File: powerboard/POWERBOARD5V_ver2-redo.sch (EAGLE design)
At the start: 37 parts, among them IC1 TPS5420, IC2 TPS5420

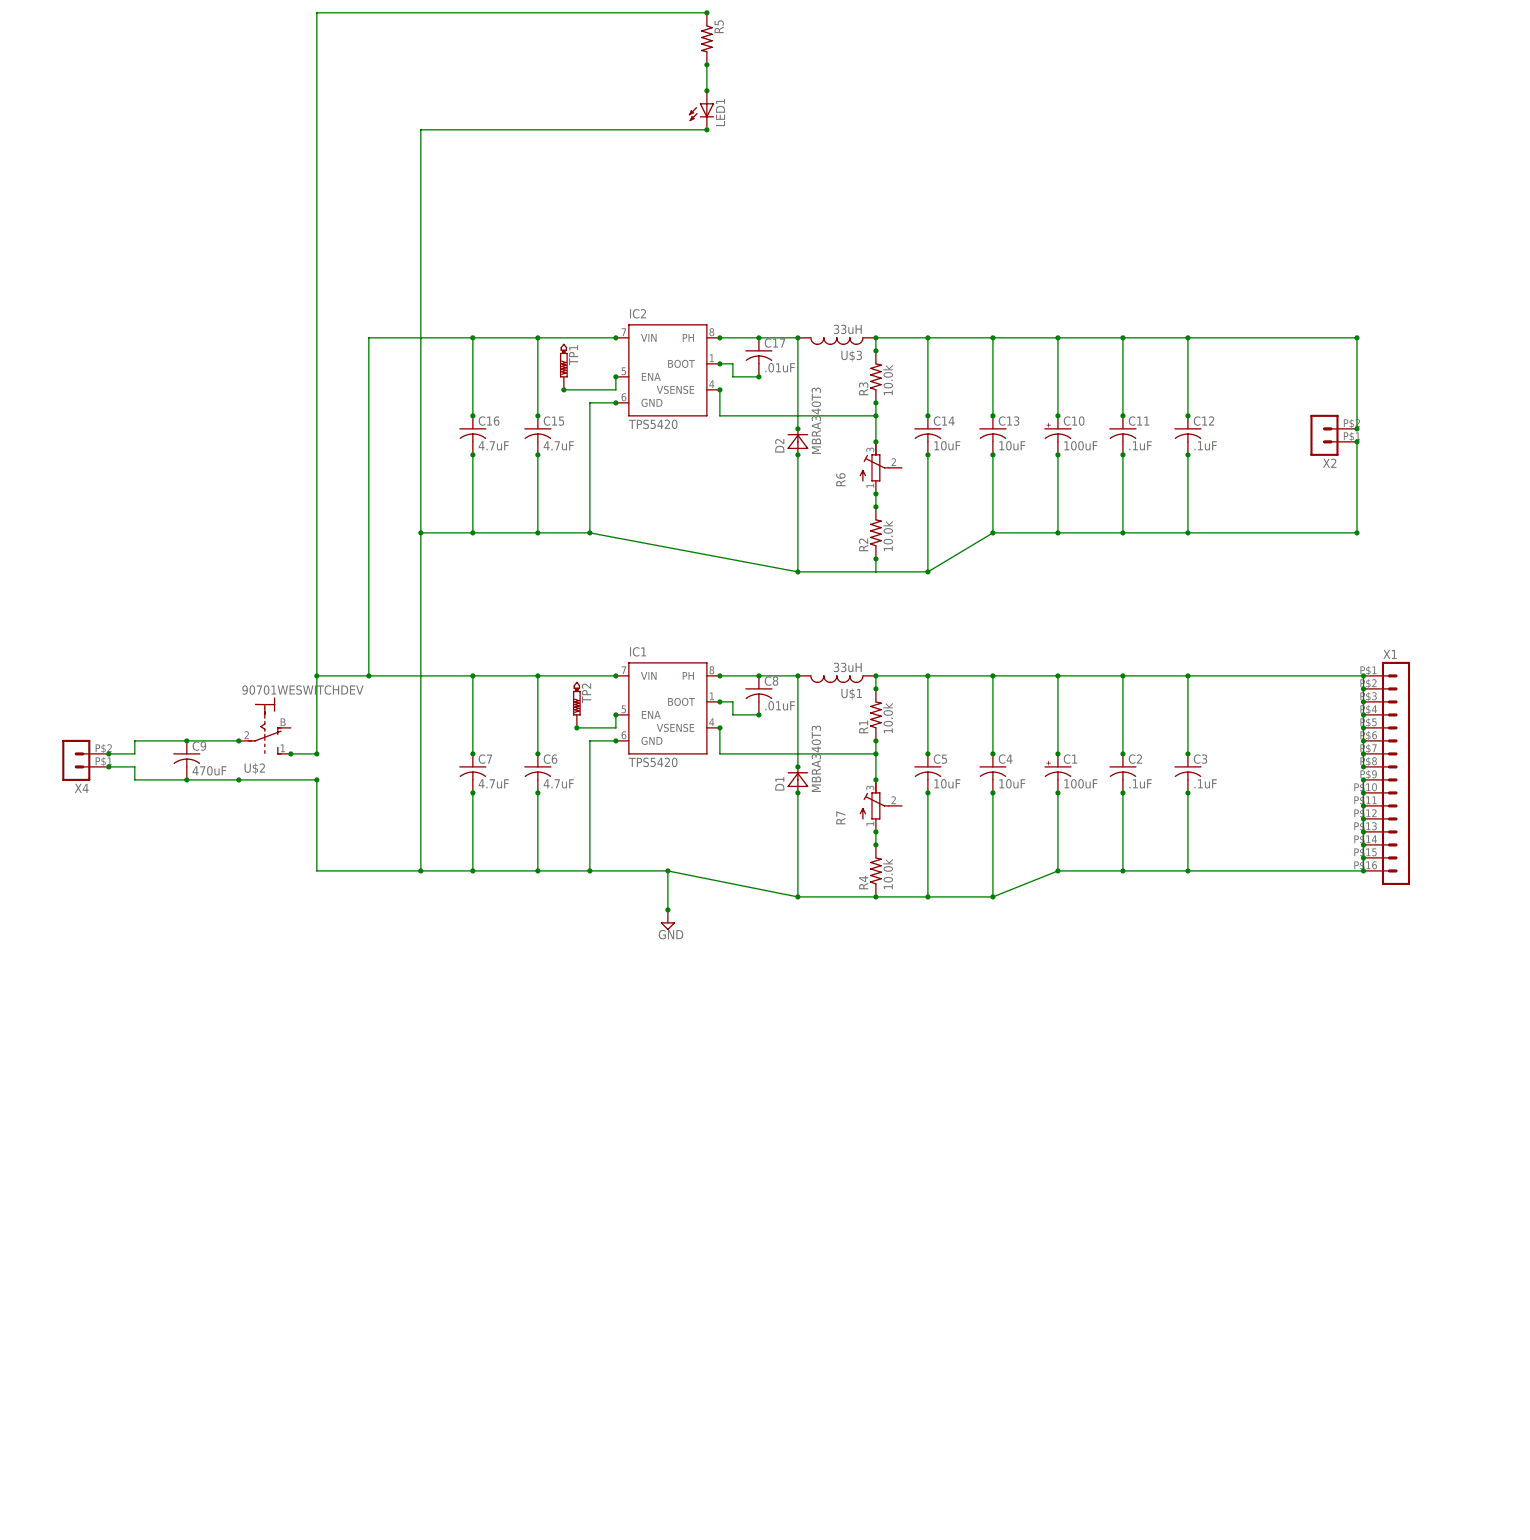
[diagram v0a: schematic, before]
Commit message: Added the 6volt rail to schematic. Board not done.
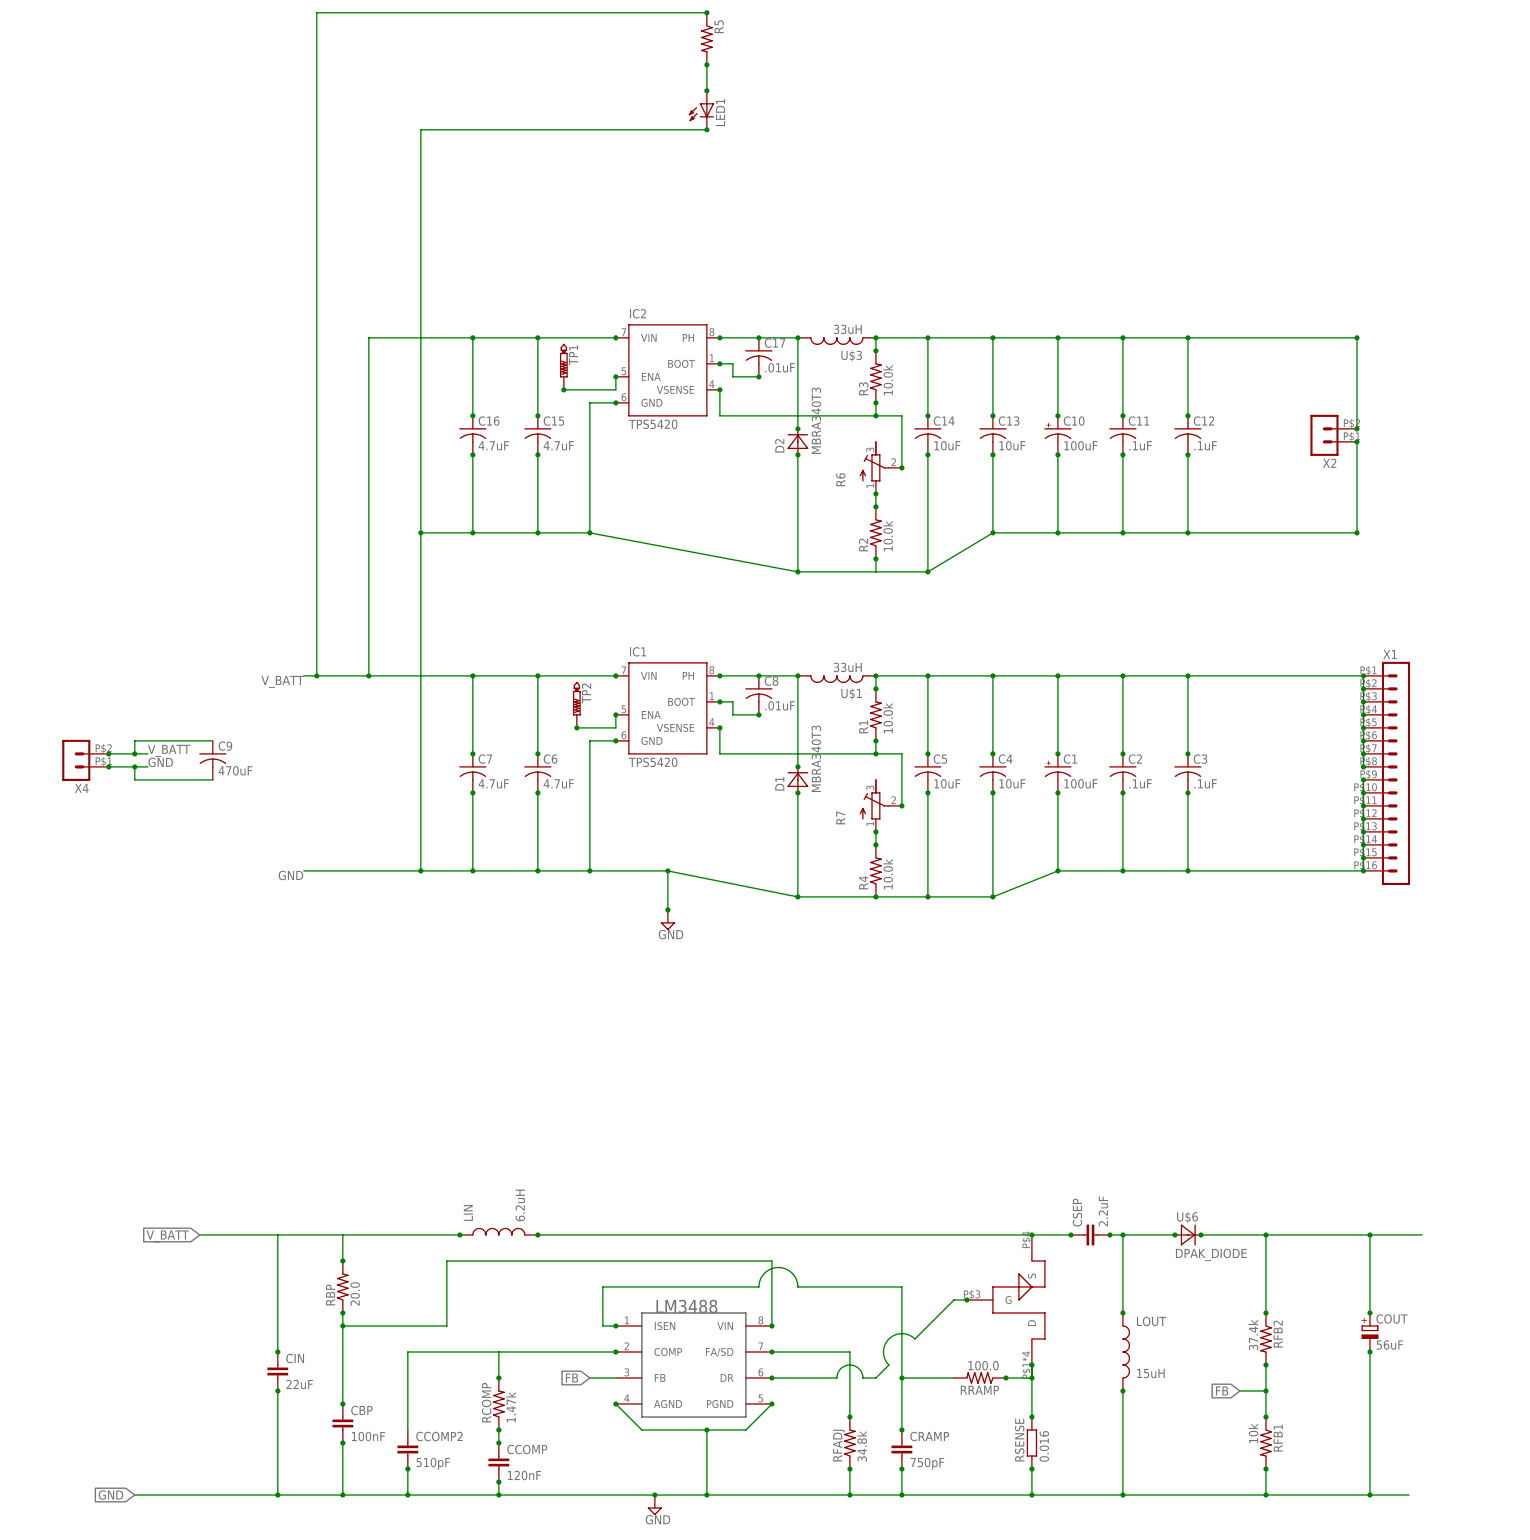
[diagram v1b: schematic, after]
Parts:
- added CBP: 100nF, rcl:C-EUC0805
- added CCOMP: 120nF, rcl:C-EUC0805
- added CCOMP2: 510pF, rcl:C-EUC0805
- added CIN: 22uF, rcl:C-EUC0805
- added COUT: 56uF, rcl:CPOL-EUSANYO_SMD_A5
- added CRAMP: 750pF, rcl:C-EUC0805
- added CSEP: 2.2uF, rcl:C-EUC0805
- added LIN: 6.2uH, SparkFun-Passives:INDUCTORSRU1038
- added LOUT: 15uH, SparkFun-Passives:INDUCTORSRU1038
- added RBP: 20.0, rcl:R-US_R0805
- added RCOMP: 1.47k, rcl:R-US_R0805
- added RFADJ: 34.8k, rcl:R-US_R0805
- added RFB1: 10k, rcl:R-US_R0805
- added RFB2: 37.4k, rcl:R-US_R0805
- added RRAMP: 100.0, rcl:R-US_R0805
- added RSENSE: 0.016, rcl:R-EU_R2512
- added U$5: P-CHANNEL20V(D-S)MOSFET, ngohara_parts:P-CHANNEL20V(D-S)MOSFET
- added U$6: DPAK_DIODE, ngohara_parts:DPAK_DIODE
- U$2: value 90701WESWITCHDEV -> LM3488; device daniel:90701WESWITCHDEV -> 40xx:LM3488
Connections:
- net N$1 renamed 5V
- net N$9 renamed 3_3V
- removed net N$3: C15.1, C16.1, C6.1, C7.1, IC1.VIN, IC2.VIN, R5.1, U$2.1
- new net FB: RFB1.1, RFB2.2, U$2.FB
- new net N$1: CCOMP.1, RCOMP.1
- new net N$20: RFADJ.2, U$2.FA/SD
- new net N$21: CRAMP.1, RRAMP.2, U$2.ISEN
- new net N$22: RRAMP.1, RSENSE.2, U$5.D
- new net N$23: U$2.DR, U$5.G
- new net N$24: CSEP.1, LIN.2, U$5.S
- new net N$25: CSEP.2, LOUT.1, U$6.A
- new net N$26: COUT.+, RFB2.1, U$6.C
- new net N$9: CBP.1, RBP.1, U$2.VIN
- new net V_BATT: C15.1, C16.1, C6.1, C7.1, C9.1, CIN.1, IC1.VIN, IC2.VIN, LIN.1, R5.1, RBP.2, X4.2
- net GND: now also CBP.2, CCOMP.2, CCOMP2.2, CIN.2, COUT.-, CRAMP.2, LOUT.2, RFADJ.1, RFB1.2, RSENSE.1, U$2.AGND, U$2.PGND
- net N$12: now also R6.S; no longer R6.E
- net N$5: now also R7.S; no longer R7.E
- net N$7: now also CCOMP2.1, RCOMP.2, U$2.COMP; no longer C9.1, U$2.2, X4.2
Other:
- moved on the sheet: C9

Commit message: Flipped board on side to fit within EagleLite's size limits
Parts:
- R2, R4: value 10.0k -> (none)
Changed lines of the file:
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@@
 <part name="R6" library="rcl" deviceset="R-TRIMM" device="3224W"/>
 <part name="R7" library="rcl" deviceset="R-TRIMM" device="3224W"/>
-<part name="R2" library="rcl" deviceset="R-US_" device="R3216" value="10.0k"/>
-<part name="R4" library="rcl" deviceset="R-US_" device="R3216" value="10.0k"/>
+<part name="R2" library="rcl" deviceset="R-US_" device="R3216"/>
+<part name="R4" library="rcl" deviceset="R-US_" device="R3216"/>
 <part name="U$2" library="40xx" deviceset="LM3488" device=""/>
 <part name="COUT" library="rcl" deviceset="CPOL-EU" device="SANYO_SMD_A5" value="56uF"/>

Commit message: Deleted TP1 and TP2 (test points) because they seem useless
-Moved parts around to reduce footprint
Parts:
- removed TP1, TP2: PTR1PAD1-13, testpad:PTR1PAD1-13
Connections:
- removed net N$4: IC2.ENA, TP1.TP
- removed net N$8: IC1.ENA, TP2.TP
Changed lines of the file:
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@@
 <part name="U$3" library="inductor-coilcraft-3" deviceset="MSS1260" device="" value="33uH"/>
 <part name="IC2" library="daniel" deviceset="TPS5420" device=""/>
-<part name="TP1" library="testpad" deviceset="PTR1" device="PAD1-13"/>
-<part name="TP2" library="testpad" deviceset="PTR1" device="PAD1-13"/>
 <part name="X4" library="con-molex-micro-fit-3_0" deviceset="HEADER_POS2_?" device="43045-0206"/>
 <part name="X1" library="con-molex-micro-fit-3_0" deviceset="HEADER_POS16_?" device="43045-1606"/>
@@
 <instance part="U$3" gate="G$1" x="63.5" y="86.36" rot="R90"/>
 <instance part="IC2" gate="P" x="30.48" y="81.28"/>
-<instance part="TP1" gate="G$1" x="10.16" y="78.74" rot="R180"/>
-<instance part="TP2" gate="G$1" x="12.7" y="12.7" rot="R180"/>
 <instance part="X4" gate="G$1" x="-83.82" y="5.08" rot="R180"/>
 <instance part="X1" gate="G$1" x="171.45" y="0"/>
@@
 </segment>
 </net>
-<net name="N$4" class="0">
-<segment>
-<pinref part="IC2" gate="P" pin="ENA"/>
-<wire x1="10.16" y1="76.2" x2="20.32" y2="76.2" width="0.1524" layer="91"/>
-<wire x1="20.32" y1="76.2" x2="20.32" y2="78.74" width="0.1524" layer="91"/>
-<junction x="20.32" y="78.74"/>
-<pinref part="TP1" gate="G$1" pin="TP"/>
-<junction x="10.16" y="76.2"/>
-</segment>
-</net>
-<net name="N$8" class="0">
-<segment>
-<pinref part="IC1" gate="P" pin="ENA"/>
-<wire x1="12.7" y1="10.16" x2="20.32" y2="10.16" width="0.1524" layer="91"/>
-<wire x1="20.32" y1="10.16" x2="20.32" y2="12.7" width="0.1524" layer="91"/>
-<junction x="20.32" y="12.7"/>
-<pinref part="TP2" gate="G$1" pin="TP"/>
-<junction x="12.7" y="10.16"/>
-</segment>
-</net>
